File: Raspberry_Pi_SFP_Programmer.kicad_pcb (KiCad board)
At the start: 2 copper layers, 65 x 56 mm, 18 parts, among them J1 RPi_GPIO, J2 SFP+, J4 Conn_02x03_Odd_Even, Q1 BC847, Q2 BC847

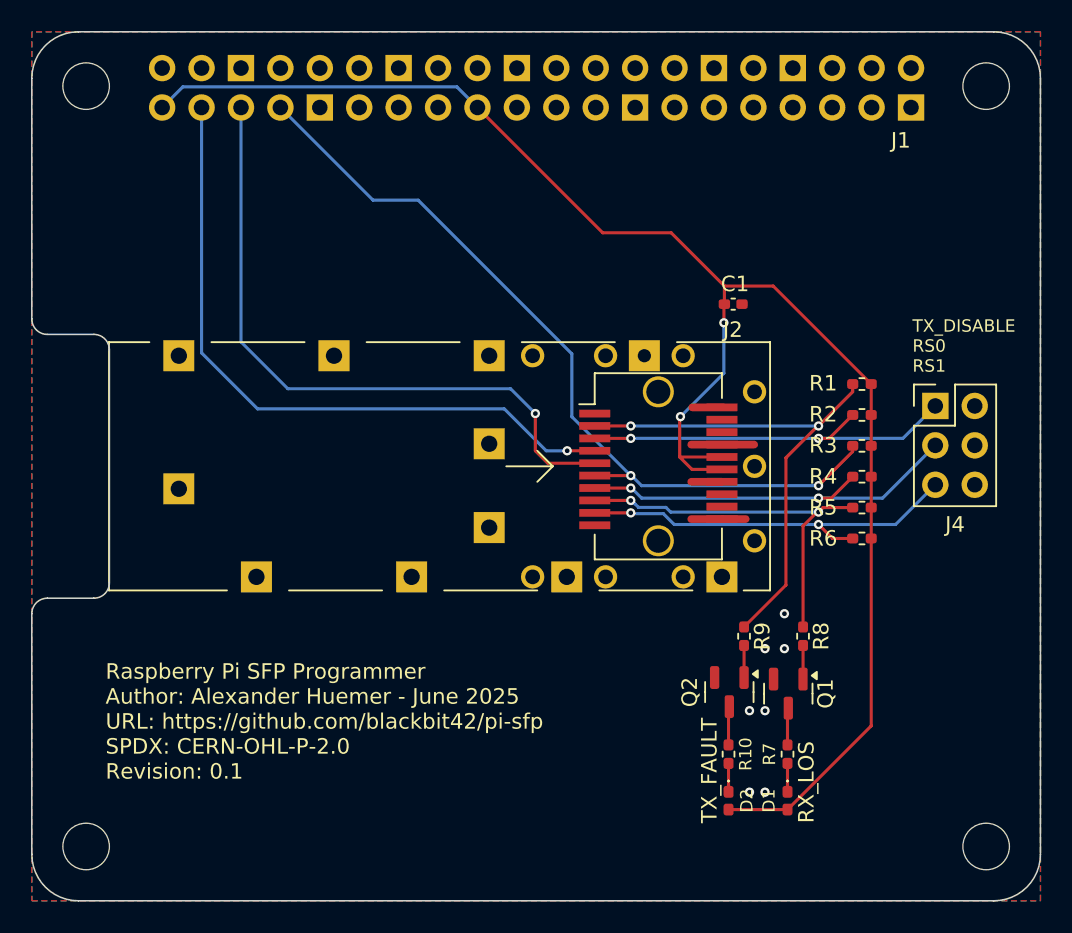
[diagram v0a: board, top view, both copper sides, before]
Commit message: Multiple improvements
Fix 3.3V rail decoupling
Derive VccT and VccR from 5V
Add power supply filter networks
Replace jumper pin header with dip switch
Add LED for MOD_ABS
Connect RX_LOS and TX_FAULT to GPIOs
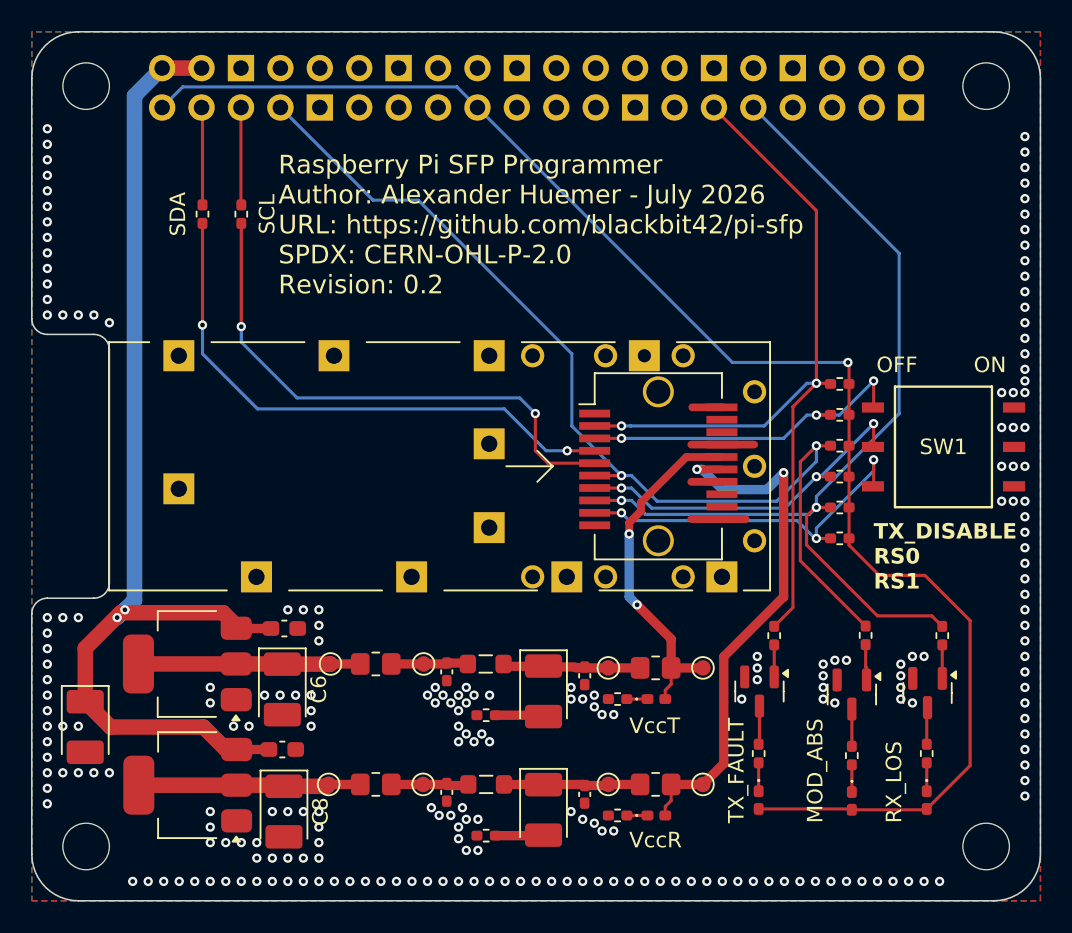
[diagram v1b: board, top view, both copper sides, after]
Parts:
- removed J4: Conn_02x03_Odd_Even, Connector_PinHeader_2.54mm:PinHeader_2x03_P2.54mm_Vertical
- added C12: 1u, Capacitor_SMD:C_0603_1608Metric_Pad1.08x0.95mm_HandSolder, F.Cu at (72.8, 92.2)
- added C13: 1u, Capacitor_SMD:C_0603_1608Metric_Pad1.08x0.95mm_HandSolder, F.Cu at (72.6, 100.0)
- added C14: 22u, Capacitor_Tantalum_SMD:CP_EIA-3528-21_Kemet-B_HandSolder, F.Cu at (59.9, 98.6)
- added C2: 0.1u, Capacitor_SMD:C_0402_1005Metric_Pad0.74x0.62mm_HandSolder, F.Cu at (83.2, 95.0)
- added C3: 22u, Capacitor_Tantalum_SMD:CP_EIA-3528-21_Kemet-B_HandSolder, F.Cu at (89.5, 103.9)
- added C4: 0.1u, Capacitor_SMD:C_0402_1005Metric_Pad0.74x0.62mm_HandSolder, F.Cu at (92.1, 95.2)
- added C5: 0.1u, Capacitor_SMD:C_0402_1005Metric_Pad0.74x0.62mm_HandSolder, F.Cu at (83.2, 102.8)
- added C6: 22u, Capacitor_Tantalum_SMD:CP_EIA-3528-21_Kemet-B_HandSolder, F.Cu at (72.6, 96.1)
- added C7: 0.1u, Capacitor_SMD:C_0402_1005Metric_Pad0.74x0.62mm_HandSolder, F.Cu at (92.1, 102.9)
- added C8: 22u, Capacitor_Tantalum_SMD:CP_EIA-3528-21_Kemet-B_HandSolder, F.Cu at (72.8, 104.0)
- added D3: LED, LED_SMD:LED_0402_1005Metric_Pad0.77x0.64mm_HandSolder, F.Cu at (109.3, 103.3)
- added D4: LED, LED_SMD:LED_0402_1005Metric_Pad0.77x0.64mm_HandSolder, F.Cu at (96.8, 96.8)
- added D5: LED, LED_SMD:LED_0402_1005Metric_Pad0.77x0.64mm_HandSolder, F.Cu at (96.8, 104.2)
- added L1: 4.7u, Inductor_SMD:L_0805_2012Metric_Pad1.05x1.20mm_HandSolder, F.Cu at (85.8, 94.5)
- added L2: 4.7u, Inductor_SMD:L_0805_2012Metric_Pad1.05x1.20mm_HandSolder, F.Cu at (85.8, 102.2)
- added Q3: BC847, Package_TO_SOT_SMD:SOT-23, F.Cu at (109.3, 96.5)
- added R11: 0.1, Resistor_SMD:R_0805_2012Metric_Pad1.20x1.40mm_HandSolder, F.Cu at (78.7, 94.5)
- added R12: 0.5, Resistor_SMD:R_0402_1005Metric_Pad0.72x0.64mm_HandSolder, F.Cu at (85.8, 97.8)
- added R13: 0.5, Resistor_SMD:R_0402_1005Metric_Pad0.72x0.64mm_HandSolder, F.Cu at (85.8, 105.6)
- added R14: 0.1, Resistor_SMD:R_0805_2012Metric_Pad1.20x1.40mm_HandSolder, F.Cu at (78.7, 102.2)
- added R15: 10k, Resistor_SMD:R_0402_1005Metric_Pad0.72x0.64mm_HandSolder, F.Cu at (110.2, 92.6)
- added R16: 3.3k, Resistor_SMD:R_0402_1005Metric_Pad0.72x0.64mm_HandSolder, F.Cu at (109.3, 100.4)
- added R17: 0.1, Resistor_SMD:R_0805_2012Metric_Pad1.20x1.40mm_HandSolder, F.Cu at (96.7, 94.7)
- added R18: 0.1, Resistor_SMD:R_0805_2012Metric_Pad1.20x1.40mm_HandSolder, F.Cu at (96.7, 102.2)
- added R19: 3.3k, Resistor_SMD:R_0402_1005Metric_Pad0.72x0.64mm_HandSolder, F.Cu at (94.2, 96.8)
- added R20: 3.3k, Resistor_SMD:R_0402_1005Metric_Pad0.72x0.64mm_HandSolder, F.Cu at (94.2, 104.2)
- added R21: 0, Resistor_SMD:R_0402_1005Metric_Pad0.72x0.64mm_HandSolder, F.Cu at (67.5, 65.5)
- added R22: 0, Resistor_SMD:R_0402_1005Metric_Pad0.72x0.64mm_HandSolder, F.Cu at (70.0, 65.5)
- added SW1: EDS03SGNNTR04Q, Raspberry_Pi_SFP_Programmer:SW_2319847_TEC, F.Cu at (115.2, 80.5)
- added TP1: TestPoint, TestPoint:TestPoint_Pad_D1.0mm, F.Cu at (75.8, 94.5)
- added TP2: TestPoint, TestPoint:TestPoint_Pad_D1.0mm, F.Cu at (81.8, 94.5)
- added TP3: TestPoint, TestPoint:TestPoint_Pad_D1.0mm, F.Cu at (75.6, 102.2)
- added TP4: TestPoint, TestPoint:TestPoint_Pad_D1.0mm, F.Cu at (81.7, 102.2)
- added TP5: TestPoint, TestPoint:TestPoint_Pad_D1.0mm, F.Cu at (93.7, 94.7)
- added TP6: TestPoint, TestPoint:TestPoint_Pad_D1.0mm, F.Cu at (99.8, 94.7)
- added TP7: TestPoint, TestPoint:TestPoint_Pad_D1.0mm, F.Cu at (93.7, 102.2)
- added TP8: TestPoint, TestPoint:TestPoint_Pad_D1.0mm, F.Cu at (99.8, 102.2)
- added U1: AMS1117-3.3, Package_TO_SOT_SMD:SOT-223-3_TabPin2, F.Cu at (66.5, 94.5)
- added U2: AMS1117-3.3, Package_TO_SOT_SMD:SOT-223-3_TabPin2, F.Cu at (66.5, 102.3)
- C1: value 1u -> 22u; footprint Capacitor_SMD:C_0402_1005Metric_Pad0.74x0.62mm_HandSolder -> Capacitor_Tantalum_SMD:CP_EIA-3528-21_Kemet-B_HandSolder
- R10, R7: value 330 -> 3.3k
- moved C1 27.8 mm to (89.5, 96.2), turned to -90 degrees
- moved D1 8.97 mm to (114.2, 103.3)
- moved Q1 8.97 mm to (114.2, 96.4)
- moved R7 8.97 mm to (114.2, 100.3)
- moved R8 8.97 mm to (115.2, 92.7)
- moved D2 1.94 mm to (103.3, 103.3)
- moved Q2 1.94 mm to (103.4, 96.3)
- moved R10 1.94 mm to (103.3, 100.3)
- moved R9 1.94 mm to (104.3, 92.7)
- moved R3 1.43 mm to (108.6, 80.4)
- moved R6 1.43 mm to (108.6, 86.4)
- moved R1 1.43 mm to (108.6, 76.4)
- moved R2 1.43 mm to (108.6, 78.4)
- moved R4 1.43 mm to (108.6, 82.4)
- moved R5 1.43 mm to (108.6, 84.4)
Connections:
- C1 pad 1: +3.3V -> Net-(C1-Pad1)
- C1 pad 2: GND -> Net-(C1-Pad2)
- J1 pad 2: unconnected-(J1-5V-Pad2) -> +5V
- J1 pad 29: unconnected-(J1-BCM5-Pad29) -> /TX_FAULT
- J1 pad 31: unconnected-(J1-BCM6-Pad31) -> /RX_LOS
- J1 pad 4: unconnected-(J1-5V-Pad4) -> +5V
- J2 pad 15: +3.3V -> VccR
- J2 pad 16: +3.3V -> VccT
- J2 pad 4: /SDA -> Net-(J2-SDA)
- J2 pad 5: /SCL -> Net-(J2-SCL)
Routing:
- net +5V: track 0.00 -> 69.4 mm, vias 0 -> 2
- net /SDA: track 43.8 -> 6.30 mm, vias 1 -> 0
- net /RX_LOS: track 25.0 -> 61.6 mm
- net Net-(J2-SDA): track 0.00 -> 36.3 mm, vias 0 -> 2
- net /SCL: track 42.5 -> 6.28 mm, vias 1 -> 0
- net Net-(J2-SCL): track 0.00 -> 35.1 mm, vias 0 -> 2
- net VccR: track 0.00 -> 34.6 mm, vias 0 -> 2
- net VccT: track 0.00 -> 22.7 mm, vias 0 -> 2
- net /TX_FAULT: track 33.0 -> 53.6 mm
- net /U2-Out: track 0.00 -> 14.4 mm
- net /U1-Out: track 0.00 -> 14.3 mm
- net /MOD_ABS: track 53.0 -> 66.3 mm
- net Net-(C3-Pad1): track 0.00 -> 8.62 mm
- net Net-(C1-Pad1): track 0.00 -> 8.06 mm
- net +3.3V: track 105.6 -> 97.7 mm, vias 2 -> 1
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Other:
- board text added: "MOD_ABS"
- board text added: "Raspberry Pi SFP Programmer Author: Alexander Huemer - July 2026 URL: https://github.com/blackbit42/pi-sfp SPDX: CERN-OHL-P-2.0 Revision: 0.2"
- board text added: "SCL"
- board text added: "SDA"
- board text added: "VccR"
- board text added: "VccT"
- board text removed: "Raspberry Pi SFP Programmer Author: Alexander Huemer - June 2025 URL: https://github.com/blackbit42/pi-sfp SPDX: CERN-OHL-P-2.0 Revision: 0.1"
